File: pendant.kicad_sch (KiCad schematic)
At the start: 6 parts, among them J1 SSD1306 OLED, J2 Extra Pins, SW1 RotaryEncoder_Switch, SW2 SW_Push, SW3 SW_Push, U1 XIAO-ESP32-S3-DIP

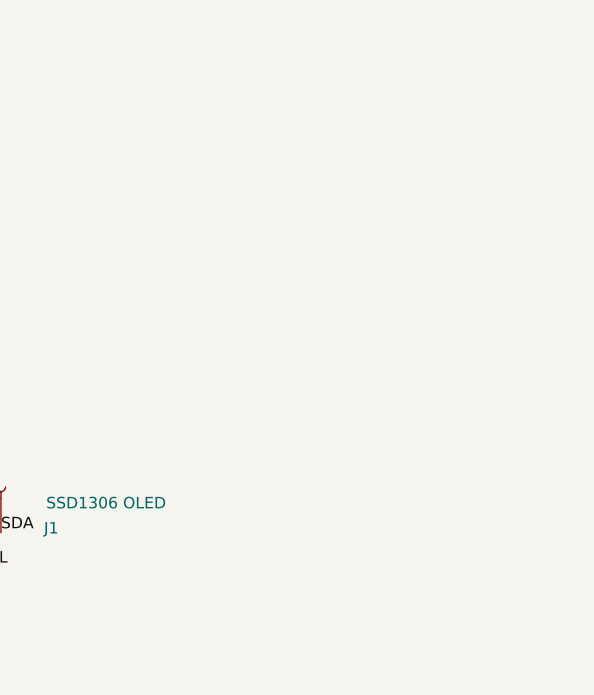
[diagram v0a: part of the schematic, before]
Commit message: Add SK6812 Mini E LEDs
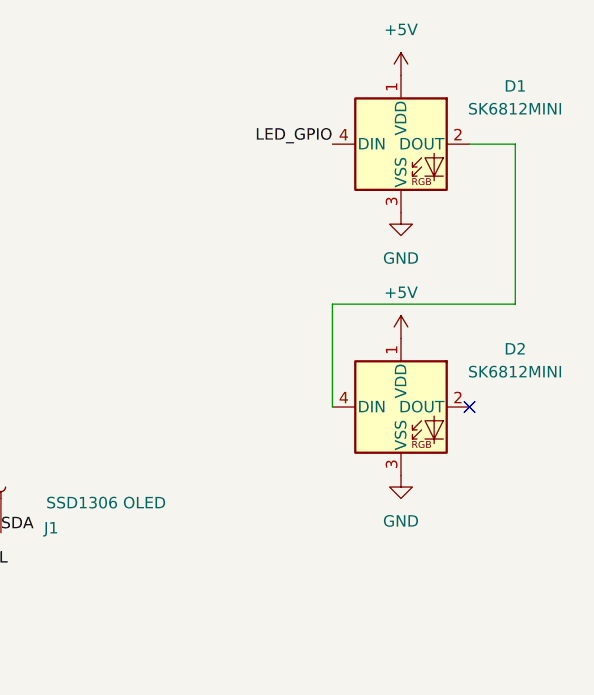
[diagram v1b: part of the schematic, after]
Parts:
- added D1, D2: SK6812MINI, LED_SMD:SK6812MINI-E_fixed, symbol LED:SK6812MINI
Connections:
- net +5V: now also D1.1 (VDD), D2.1 (VDD)
- net GND: now also D1.3 (VSS), D2.3 (VSS)
- new net: D1.2 (DOUT), D2.4 (DIN)
- new net LED_GPIO: D1.4 (DIN)
- no-connect marks 0 -> 1
